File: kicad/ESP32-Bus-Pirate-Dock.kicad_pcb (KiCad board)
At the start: 4 copper layers, 80 x 73.7 mm, 36 parts, among them CN1 HX25418-10WA, J1 Conn_01x10V, J2 Conn_01x22, J3 Conn_01x22, J4 Conn_02x03, J5 Conn_01x22, J6 Conn_01x22, J7 Conn_01x22, Q1 2N7002, Q2 2N7002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

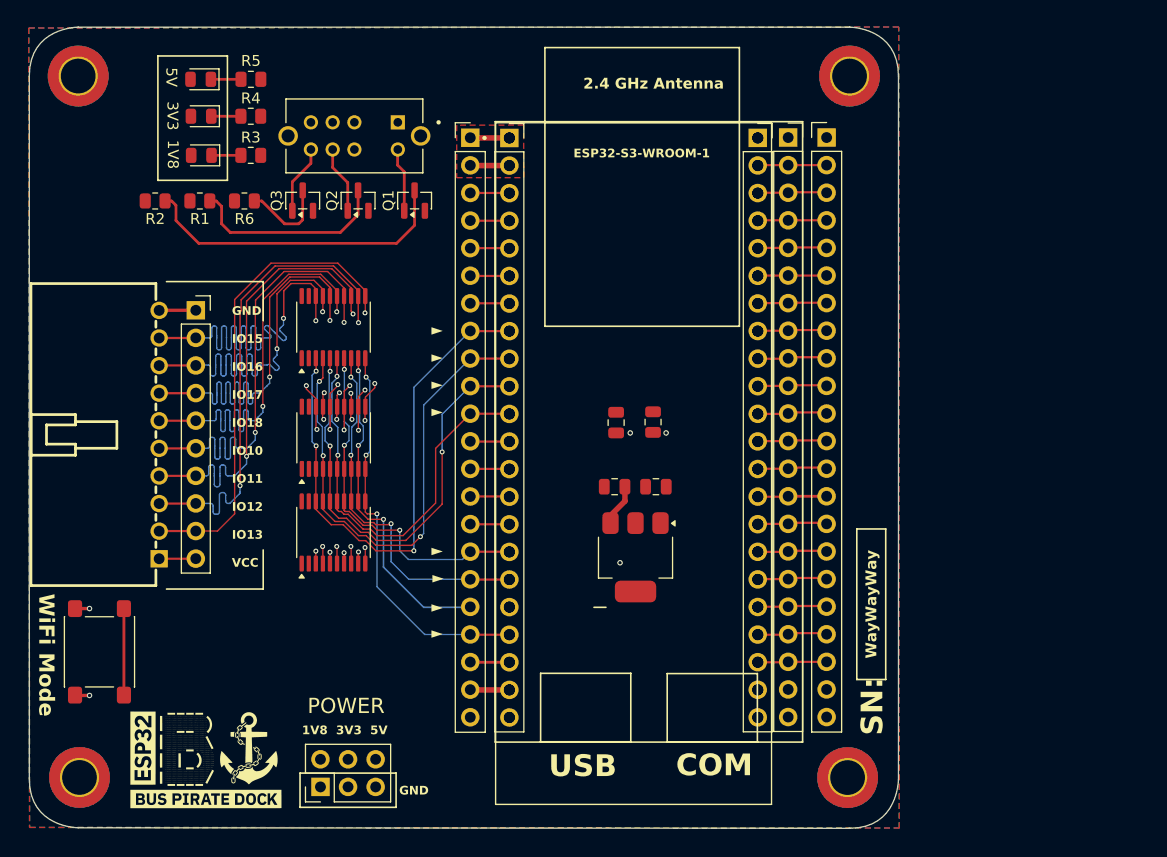
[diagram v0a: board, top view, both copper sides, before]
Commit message: Fixed board outline
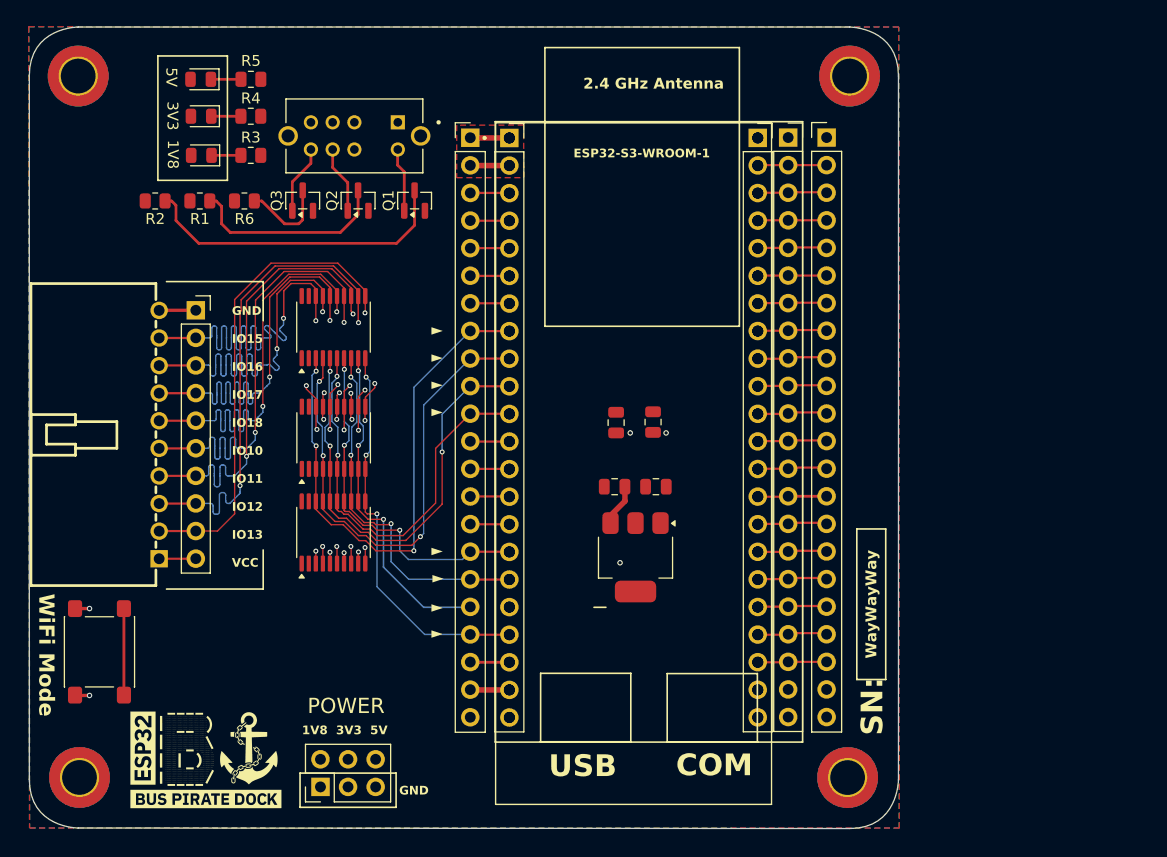
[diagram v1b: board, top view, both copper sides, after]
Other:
- board size 80 x 73.7 mm -> 80 x 73.8 mm
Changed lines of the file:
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@@
 		(layer "F.SilkS")
 	)
-	(gr_curve
-		(pts
-			(xy 203.7 64.8) (xy 203.7 60.3) (xy 199.2 60.3) (xy 199.2 60.3)
-		)
+	(gr_line
+		(start 203.7 129.56202)
+		(end 203.7 64.79)
 		(stroke
 			(width 0.05)
-			(type default)
+			(type solid)
 		)
 		(layer "Edge.Cuts")
@@
 	(gr_curve
 		(pts
-			(xy 123.7 129.49) (xy 123.7 133.99) (xy 128.2 133.99) (xy 128.2 133.99)
+			(xy 199.2 134.06202) (xy 203.7 134.06202) (xy 203.7 129.56202) (xy 203.7 129.56202)
 		)
 		(stroke
@@
 		(layer "Edge.Cuts")
 	)
-	(gr_line
-		(start 123.7 129.475)
-		(end 123.7 64.8)
+	(gr_curve
+		(pts
+			(xy 203.7 64.79) (xy 203.7 60.29) (xy 199.2 60.29) (xy 199.2 60.29)
+		)
 		(stroke
 			(width 0.05)
-			(type solid)
+			(type default)
 		)
 		(layer "Edge.Cuts")
 	)
-	(gr_line
-		(start 203.7 129.525)
-		(end 203.7 64.8)
+	(gr_curve
+		(pts
+			(xy 123.7 129.515) (xy 123.7 134.015) (xy 128.2 134.015) (xy 128.2 134.015)
+		)
 		(stroke
 			(width 0.05)
-			(type solid)
+			(type default)
 		)
 		(layer "Edge.Cuts")
@@
 	(gr_curve
 		(pts
-			(xy 123.7 64.8) (xy 123.7 60.3) (xy 128.2 60.3) (xy 128.2 60.3)
+			(xy 123.7 64.79) (xy 123.7 60.29) (xy 128.2 60.29) (xy 128.2 60.29)
 		)
 		(stroke
@@
 	)
 	(gr_line
-		(start 199.19 134.04)
-		(end 128.19 133.99298)
+		(start 199.2 134.06202)
+		(end 128.2 134.015)
 		(stroke
 			(width 0.05)
@@
 		(layer "Edge.Cuts")
 	)
-	(gr_curve
-		(pts
-			(xy 199.2 134.04) (xy 203.7 134.04) (xy 203.7 129.54) (xy 203.7 129.54)
-		)
+	(gr_line
+		(start 123.7 129.515)
+		(end 123.7 64.79)
 		(stroke
 			(width 0.05)
-			(type default)
+			(type solid)
 		)
 		(layer "Edge.Cuts")
 	)
 	(gr_line
-		(start 199.2 60.3)
-		(end 128.2 60.3)
+		(start 199.2 60.29)
+		(end 128.2 60.29)
 		(stroke
 			(width 0.05)
@@
 		(polygon
 			(pts
-				(xy 123.725 133.96) (xy 203.45 134.01) (xy 203.775 134.03) (xy 203.725 60.275) (xy 123.65 60.375)
+				(xy 123.725 134.01) (xy 203.468347 134.028347) (xy 203.775 134.03) (xy 203.725 60.275) (xy 123.65 60.26)
 			)
 		)

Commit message: Eliminated old traces
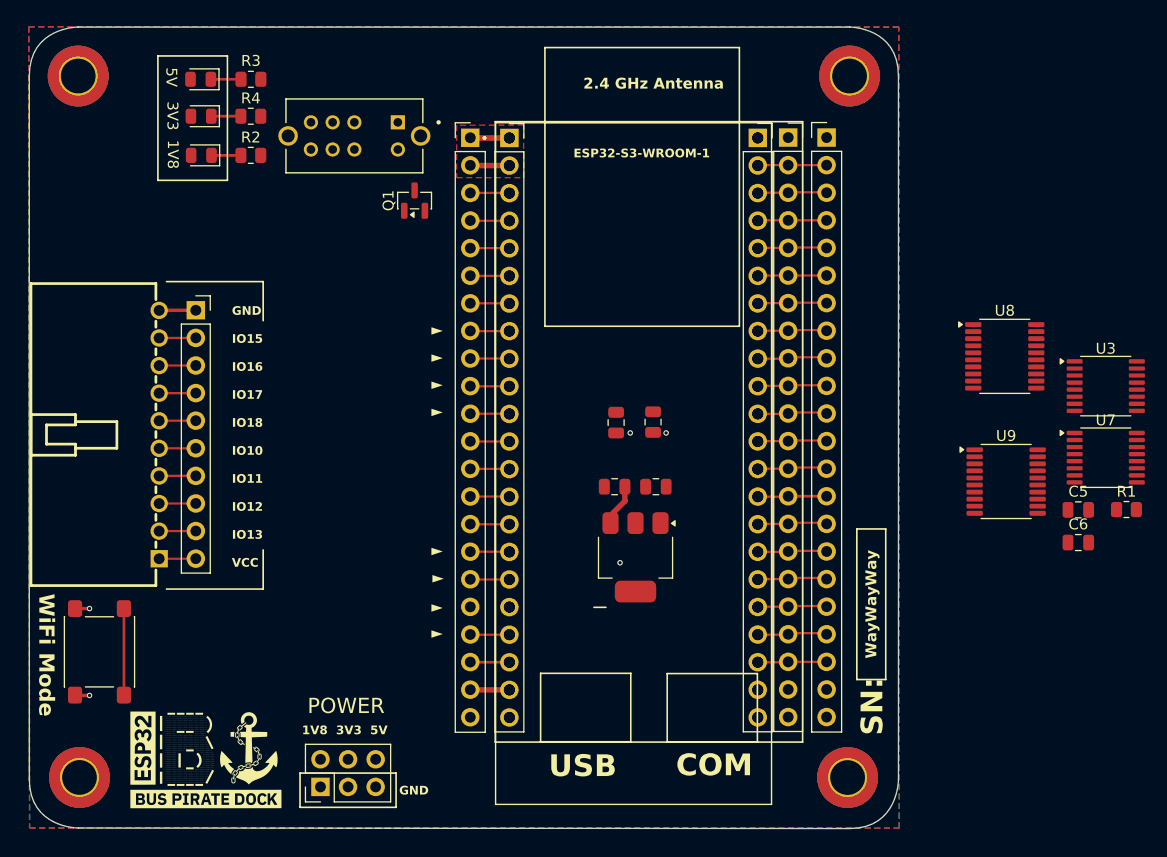
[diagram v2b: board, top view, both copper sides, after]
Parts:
- removed Q2, Q3: 2N7002, Package_TO_SOT_SMD:SOT-23
- removed the R2 at (135.3, 76.3)
- removed R6: 200k, Resistor_SMD:R_0805_2012Metric
- removed U4, U5, U6: LSF0108PW, Package_SO:TSSOP-20_4.4x6.5mm_P0.65mm
- added C5: 0.1u, Capacitor_SMD:C_0805_2012Metric, F.Cu at (220.3, 104.7)
- added C6: 0.1u, Capacitor_SMD:C_0805_2012Metric, F.Cu at (220.3, 107.7)
- added U3: TMUX1574PW, Package_SO:TSSOP-16_4.4x5mm_P0.65mm, F.Cu at (222.8, 93.3)
- added U7: TMUX1574PW, Package_SO:TSSOP-16_4.4x5mm_P0.65mm, F.Cu at (222.8, 99.9)
- added U8: TXS0108EPW, Package_SO:Texas_PW0020A_TSSOP-20_4.4x6.5mm_P0.65mm, F.Cu at (213.5, 90.6)
- added U9: TXS0108EPW, Package_SO:Texas_PW0020A_TSSOP-20_4.4x6.5mm_P0.65mm, F.Cu at (213.6, 102.1)
- D1: value LED -> BLUE
- D2: renamed from D3; value LED -> ORANGE
- D3: renamed from D2; value LED -> RED
- R1: value 200k -> 10k
- moved R1 89.9 mm to (224.7, 104.7), turned to 0 degrees
- renumbered R3 to R2, R5 to R3
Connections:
- net /Voltage Level Translator/D1 renamed /Voltage Level Translator/D1_K
- net /Voltage Level Translator/D2 renamed /Voltage Level Translator/D3_K
- net /Voltage Level Translator/D3 renamed /Voltage Level Translator/D2_K
- D1 pad 2: +3.3V -> /Voltage Level Translator/D1_A
- D2 pad 2: +3.3V -> /Voltage Level Translator/D2_A
- D3 pad 2: +3.3V -> /Voltage Level Translator/D3_A
- Q1 pad 1: /Voltage Level Translator/Gate_1 -> GND
- Q1 pad 3: /Voltage Level Translator/RefB_1 -> /Voltage Level Translator/SEL
- R1 pad 1: /Voltage Level Translator/RefB_2 -> /Voltage Level Translator/SEL
- R2 pad 2: /Voltage Level Translator/Gate_1 -> GND
- R3 pad 2: /Voltage Level Translator/Gate_3 -> GND
- R4 pad 2: /Voltage Level Translator/Gate_2 -> GND
- S1 pad 5: /Voltage Level Translator/Gate_1 -> /Voltage Level Translator/D1_A
- S1 pad 6: GND -> +3.3V
- S1 pad 7: /Voltage Level Translator/Gate_2 -> /Voltage Level Translator/D2_A
- S1 pad 8: /Voltage Level Translator/Gate_3 -> /Voltage Level Translator/D3_A
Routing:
- net IO15: track 68.8 -> 3.38 mm, vias 5 -> 0
- net IO17: track 68.7 -> 3.38 mm, vias 5 -> 0
- net IO12: track 68.2 -> 3.38 mm, vias 5 -> 0
- net IO13: track 68.1 -> 3.38 mm, vias 4 -> 0
- net IO18: track 67.8 -> 3.38 mm, vias 5 -> 0
- net IO10: track 67.4 -> 3.38 mm, vias 5 -> 0
- net IO11: track 66.4 -> 3.38 mm, vias 5 -> 0
- net IO16: track 66.3 -> 3.38 mm, vias 5 -> 0
- net GPIO15: track 51.1 -> 3.82 mm, vias 3 -> 0
- net GPIO16: track 47.2 -> 3.85 mm, vias 3 -> 0
- net GPIO17: track 43.2 -> 3.82 mm, vias 3 -> 0
- net GPIO18: track 39.1 -> 3.85 mm, vias 2 -> 0
- net GPIO13: track 36.6 -> 3.82 mm, vias 3 -> 0
- net GPIO12: track 30.9 -> 0.00 mm, vias 3 -> 0
- net GPIO11: track 34.0 -> 3.82 mm, vias 3 -> 0
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
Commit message: Updated wiring
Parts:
- moved U7 74.6 mm to (148.3, 103.2), turned to -90 degrees
- moved U3 74.4 mm to (148.3, 92.6), turned to -90 degrees
- moved U8 55.8 mm to (157.7, 92.4), turned to 180 degrees
- moved U9 55.6 mm to (158.0, 103.1)
- moved C1 2.71 mm to (180.3, 102.6)
- moved C2 2.71 mm to (183.8, 96.6)
- moved C3 2.71 mm to (184.1, 102.6)
- moved J2 2.71 mm to (199.8, 70.4)
- moved J3 2.71 mm to (167.0, 70.4)
- moved J6 2.71 mm to (170.6, 70.5)
- moved J7 2.71 mm to (193.5, 70.5)
- moved U1 2.71 mm to (182.0, 100.4)
- moved U2 2.71 mm to (182.2, 109.1)
- moved C4 2.71 mm to (180.4, 96.7)
- moved J5 2.71 mm to (196.3, 70.4)
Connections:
- U8 pad 16: unconnected-(U8-B4-Pad16) -> /Voltage Level Translator/IO18_H
- U9 pad 5: unconnected-(U9-A4-Pad5) -> /Voltage Level Translator/IO18_L
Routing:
- net IO15: track 3.38 -> 14.6 mm
- net IO13: track 3.38 -> 14.1 mm
- net IO10: track 3.38 -> 14.1 mm
- net /Voltage Level Translator/IO11_L: track 0.00 -> 10.3 mm
- net /Voltage Level Translator/IO16_H: track 0.00 -> 9.89 mm
- net /Voltage Level Translator/IO17_H: track 0.00 -> 9.63 mm, vias 0 -> 2
- net /Voltage Level Translator/IO15_H: track 0.00 -> 9.63 mm, vias 0 -> 2
- net /Voltage Level Translator/IO12_L: track 0.00 -> 9.03 mm
- net IO12: track 3.38 -> 11.7 mm
- net /Voltage Level Translator/IO13_L: track 0.00 -> 8.12 mm
- net /Voltage Level Translator/IO18_H: track 0.00 -> 7.66 mm, vias 0 -> 2
- net /Voltage Level Translator/IO10_L: track 0.00 -> 7.65 mm
- net IO16: track 3.38 -> 9.93 mm
- net /Voltage Level Translator/IO11_H: track 0.00 -> 1.16 mm, vias 0 -> 1
- net /Voltage Level Translator/IO13_H: track 0.00 -> 1.14 mm, vias 0 -> 1
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
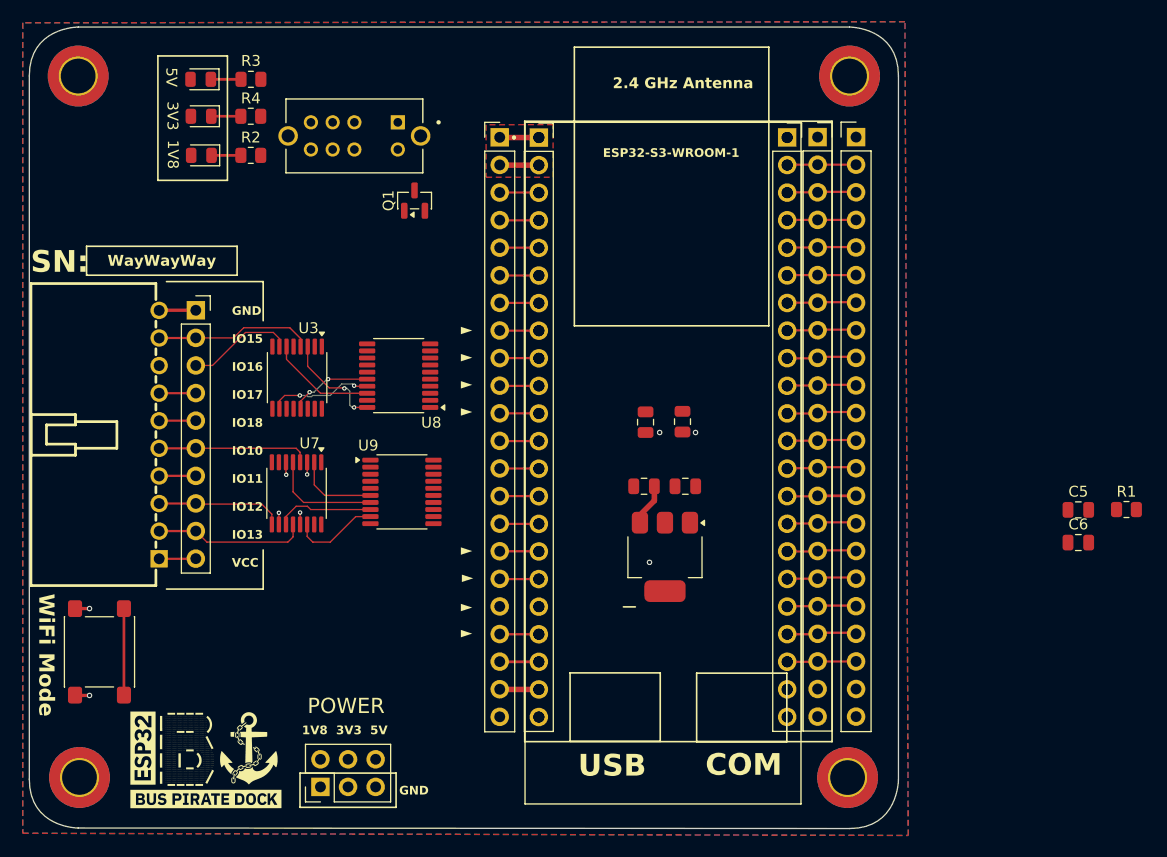
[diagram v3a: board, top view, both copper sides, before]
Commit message: Partial re-wiring
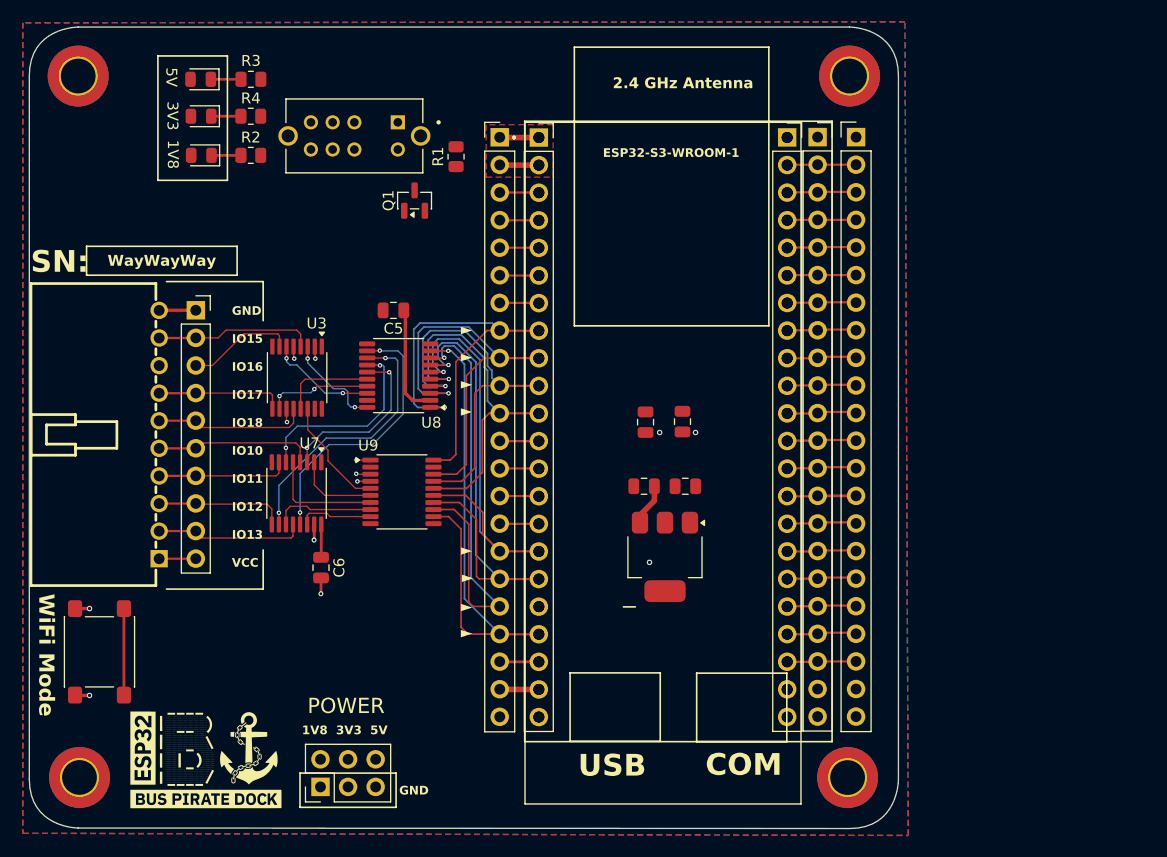
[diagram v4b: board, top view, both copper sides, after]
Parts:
- moved C6 69.7 mm to (150.6, 110.0), turned to -90 degrees
- moved R1 69.7 mm to (163.0, 72.2), turned to 90 degrees
- moved C5 65.7 mm to (157.2, 86.4), turned to 180 degrees
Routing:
- net GPIO13: track 3.82 -> 49.5 mm, vias 0 -> 1
- net GPIO12: track 0.00 -> 43.1 mm, vias 0 -> 1
- net GPIO11: track 3.82 -> 45.1 mm, vias 0 -> 1
- net GPIO10: track 3.85 -> 41.3 mm, vias 0 -> 1
- net GPIO15: track 3.82 -> 39.4 mm, vias 0 -> 1
- net GPIO16: track 3.85 -> 37.9 mm, vias 0 -> 1
- net GPIO17: track 3.82 -> 35.7 mm, vias 0 -> 1
- net GPIO18: track 3.85 -> 34.6 mm, vias 0 -> 1
- net /Voltage Level Translator/IO13_H: track 1.14 -> 25.3 mm, vias 1 -> 2
- net /Voltage Level Translator/IO12_H: track 1.08 -> 24.9 mm, vias 1 -> 2
- net /Voltage Level Translator/IO11_H: track 1.16 -> 18.0 mm, vias 1 -> 2
- net /Voltage Level Translator/IO16_L: track 0.00 -> 15.7 mm, vias 0 -> 2
- net /Voltage Level Translator/IO10_H: track 1.12 -> 16.1 mm, vias 1 -> 2
- net /Voltage Level Translator/IO15_L: track 0.00 -> 13.9 mm, vias 0 -> 2
- net +3.3V: track 7.22 -> 20.5 mm
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- added copper zone on In1.Cu, net GND
- added copper zone on In2.Cu, net GND

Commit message: Wired everything
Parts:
- removed U1: ESP32-S3-DEVKITC-1-N8R2, ESP32-S3-DEVKITC-1-N8R2:XCVR_ESP32-S3-DEVKITC-1-N8R2
- moved C2 15.8 mm to (176.7, 110.8), turned to 180 degrees
- moved Q1 13.3 mm to (145.9, 76.5), turned to 0 degrees
- moved R1 12.1 mm to (151.6, 76.4), turned to 0 degrees
- moved C4 11.3 mm to (176.6, 107.4), turned to 180 degrees
- moved S1 1.74 mm to (155.3, 70.1)
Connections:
- U8 pad 10: unconnected-(U8-OE-Pad10) -> +3.3V
- U9 pad 10: unconnected-(U9-OE-Pad10) -> +3.3V
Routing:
- net +1V8: track 0.00 -> 119.8 mm, vias 1 -> 3
- net +5V: track 7.99 -> 111.0 mm, vias 0 -> 2
- net +3.3V: track 20.5 -> 120.2 mm, vias 0 -> 2
- net GPIO0: track 14.3 -> 84.7 mm
- net VTARGET: track 3.38 -> 65.3 mm, vias 0 -> 1
- net /Voltage Level Translator/SEL: track 0.00 -> 35.9 mm, vias 0 -> 2
- net /Voltage Level Translator/D1_A: track 0.00 -> 28.5 mm, vias 0 -> 1
- net GND: track 8.98 -> 35.6 mm, vias 6 -> 30
- net /Voltage Level Translator/D2_A: track 0.00 -> 18.2 mm
- net /Voltage Level Translator/D3_A: track 0.00 -> 14.7 mm
- added copper zone on F.Cu, net +1V8
